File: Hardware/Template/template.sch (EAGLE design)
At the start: 24 parts, among them J1 10144517-042802LF, J2 10144518-041802LF, J3 10144517-042802LF, J4 10144518-041802LF, J6 2X5_0.05_SWD, U6 NCV8170AXV330T2G, U7 ATA6561-GAQW-N

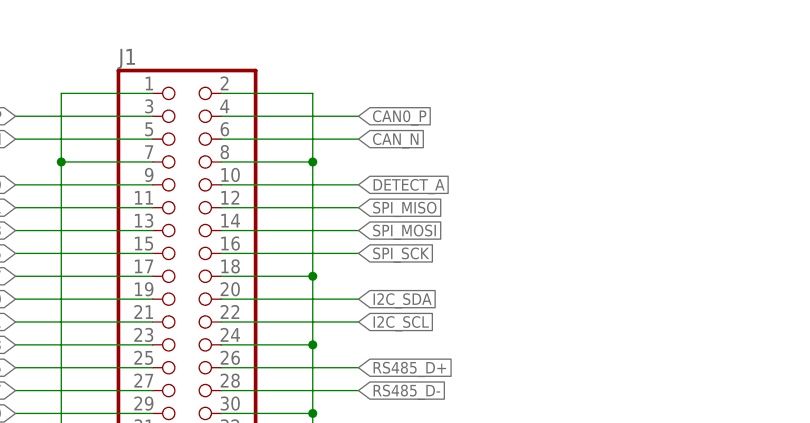
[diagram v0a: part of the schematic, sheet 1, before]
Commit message: fixed power rail naming in template and added inventor drawing
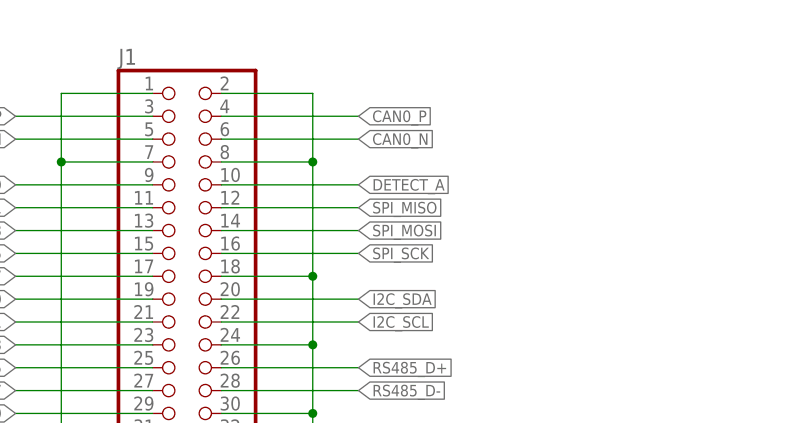
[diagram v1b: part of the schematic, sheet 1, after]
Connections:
- new net +12V: J3.17, J3.19, J3.21, J3.23, J3.25, J3.27, J3.29, J4.17, J4.19, J4.21, J4.23, J4.25, J4.27, J4.29
- net +5V: no longer J3.17, J3.19, J3.21, J3.23, J3.25, J3.27, J3.29, J4.17, J4.19, J4.21, J4.23, J4.25, J4.27, J4.29
- net CAN0_N: now also J1.6
- net CAN_N: no longer J1.6
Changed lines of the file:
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@@
 <?xml version="1.0" encoding="utf-8"?>
 <!DOCTYPE eagle SYSTEM "eagle.dtd">
-<eagle version="9.5.2">
+<eagle version="9.6.0">
 <drawing>
 <settings>
-<setting alwaysvectorfont="no"/>
+<setting alwaysvectorfont="yes"/>
 <setting verticaltext="up"/>
 </settings>
@@
 <net name="CAN_N" class="0">
 <segment>
-<wire x1="38.1" y1="187.96" x2="53.34" y2="187.96" width="0.1524" layer="91"/>
-<label x="53.34" y="187.96" size="1.27" layer="95" xref="yes"/>
-<pinref part="J1" gate="A" pin="6"/>
-</segment>
-<segment>
 <pinref part="U7" gate="G$1" pin="CANL"/>
 <label x="17.78" y="43.18" size="1.27" layer="95" rot="MR0" xref="yes"/>
@@
 <pinref part="J2" gate="A" pin="6"/>
 </segment>
+<segment>
+<wire x1="38.1" y1="187.96" x2="53.34" y2="187.96" width="0.1524" layer="91"/>
+<label x="53.34" y="187.96" size="1.27" layer="95" xref="yes"/>
+<pinref part="J1" gate="A" pin="6"/>
+</segment>
 </net>
 <net name="+5V" class="0">
@@
 <pinref part="P+3" gate="1" pin="+5V"/>
 </segment>
+<segment>
+<wire x1="228.6" y1="149.86" x2="228.6" y2="152.4" width="0.1524" layer="91"/>
+<wire x1="228.6" y1="152.4" x2="228.6" y2="154.94" width="0.1524" layer="91"/>
+<wire x1="228.6" y1="154.94" x2="228.6" y2="157.48" width="0.1524" layer="91"/>
+<wire x1="228.6" y1="157.48" x2="223.52" y2="157.48" width="0.1524" layer="91"/>
+<pinref part="J3" gate="A" pin="31"/>
+<wire x1="228.6" y1="157.48" x2="238.76" y2="157.48" width="0.1524" layer="91"/>
+<junction x="228.6" y="157.48"/>
+<pinref part="J3" gate="A" pin="33"/>
+<wire x1="238.76" y1="154.94" x2="228.6" y2="154.94" width="0.1524" layer="91"/>
+<junction x="228.6" y="154.94"/>
+<pinref part="J3" gate="A" pin="35"/>
+<wire x1="238.76" y1="152.4" x2="228.6" y2="152.4" width="0.1524" layer="91"/>
+<junction x="228.6" y="152.4"/>
+<pinref part="J3" gate="A" pin="37"/>
+<wire x1="238.76" y1="149.86" x2="228.6" y2="149.86" width="0.1524" layer="91"/>
+<pinref part="P+6" gate="1" pin="+5V"/>
+</segment>
+</net>
+<net name="+12V" class="0">
 <segment>
 <wire x1="228.6" y1="175.26" x2="223.52" y2="175.26" width="0.1524" layer="91"/>
@@
 <pinref part="P+2" gate="1" pin="+12V"/>
 </segment>
-<segment>
-<wire x1="228.6" y1="149.86" x2="228.6" y2="152.4" width="0.1524" layer="91"/>
-<wire x1="228.6" y1="152.4" x2="228.6" y2="154.94" width="0.1524" layer="91"/>
-<wire x1="228.6" y1="154.94" x2="228.6" y2="157.48" width="0.1524" layer="91"/>
-<wire x1="228.6" y1="157.48" x2="223.52" y2="157.48" width="0.1524" layer="91"/>
-<pinref part="J3" gate="A" pin="31"/>
-<wire x1="228.6" y1="157.48" x2="238.76" y2="157.48" width="0.1524" layer="91"/>
-<junction x="228.6" y="157.48"/>
-<pinref part="J3" gate="A" pin="33"/>
-<wire x1="238.76" y1="154.94" x2="228.6" y2="154.94" width="0.1524" layer="91"/>
-<junction x="228.6" y="154.94"/>
-<pinref part="J3" gate="A" pin="35"/>
-<wire x1="238.76" y1="152.4" x2="228.6" y2="152.4" width="0.1524" layer="91"/>
-<junction x="228.6" y="152.4"/>
-<pinref part="J3" gate="A" pin="37"/>
-<wire x1="238.76" y1="149.86" x2="228.6" y2="149.86" width="0.1524" layer="91"/>
-<pinref part="P+6" gate="1" pin="+5V"/>
-</segment>
-</net>
+</net>

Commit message: sims and some other stuff...
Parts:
- removed F1: (no value), adafruit:PTCFUSE-1206
- removed U$13, U$9: WIRE-PAD, Wire Pads:WIRE-PAD
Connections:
- removed net +V_BAT_INT: F1.2
- removed net N$16: F1.1, U$13.TP
- net PGND: no longer U$9.TP
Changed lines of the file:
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@@
 <part name="J2" library="BergStak" library_urn="urn:adsk.eagle:library:14049968" deviceset="10144518-04" device="1802LF" package3d_urn="urn:adsk.eagle:package:14050130/2"/>
 <part name="U$12" library="Supply" deviceset="SHIELD" device=""/>
-<part name="U$9" library="Wire Pads" deviceset="WIRE-PAD" device=""/>
-<part name="U$13" library="Wire Pads" deviceset="WIRE-PAD" device=""/>
-<part name="F1" library="adafruit" library_urn="urn:adsk.eagle:library:420" deviceset="PTCFUSE" device="-1206" package3d_urn="urn:adsk.eagle:package:6240569/1"/>
 <part name="R8" library="rcl" library_urn="urn:adsk.eagle:library:334" deviceset="R-US_" device="R0402" package3d_urn="urn:adsk.eagle:package:23547/3"/>
 <part name="U$14" library="Supply" deviceset="SHIELD" device=""/>
@@
 <part name="U$26" library="Supply" deviceset="PGND" device=""/>
 <part name="U$27" library="Supply" deviceset="DGND" device=""/>
-<part name="U$28" library="Supply" deviceset="PGND" device=""/>
 <part name="U$29" library="Supply" deviceset="DGND" device=""/>
 <part name="U$30" library="Supply" deviceset="DGND" device=""/>
@@
 <attribute name="VALUE" x="22.86" y="68.58" size="1.778" layer="96" rot="MR90"/>
 </instance>
-<instance part="U$9" gate="G$1" x="22.86" y="12.7" smashed="yes">
-<attribute name="NAME" x="21.59" y="13.97" size="1.778" layer="95"/>
-</instance>
-<instance part="U$13" gate="G$1" x="22.86" y="22.86" smashed="yes">
-<attribute name="NAME" x="21.59" y="24.13" size="1.778" layer="95"/>
-</instance>
-<instance part="F1" gate="G$1" x="33.02" y="15.24" smashed="yes">
-<attribute name="VALUE" x="29.21" y="13.97" size="1.778" layer="96"/>
-<attribute name="NAME" x="29.21" y="20.32" size="1.778" layer="95"/>
-</instance>
 <instance part="R8" gate="G$1" x="228.6" y="63.5" smashed="yes">
 <attribute name="NAME" x="224.79" y="64.9986" size="1.778" layer="95"/>
@@
 <attribute name="NAME" x="23.9014" y="44.45" size="1.778" layer="95" rot="R90"/>
 <attribute name="VALUE" x="28.702" y="44.45" size="1.778" layer="96" rot="R90"/>
-</instance>
-<instance part="U$28" gate="G$1" x="22.86" y="7.62" smashed="yes">
-<attribute name="VALUE" x="20.32" y="5.08" size="1.778" layer="96"/>
 </instance>
 <instance part="U$29" gate="G$1" x="93.98" y="33.02" smashed="yes">
@@
 </segment>
 </net>
-<net name="+V_BAT_INT" class="0">
-<segment>
-<label x="50.8" y="17.78" size="1.27" layer="95" xref="yes"/>
-<wire x1="38.1" y1="17.78" x2="50.8" y2="17.78" width="0.1524" layer="91"/>
-<pinref part="F1" gate="G$1" pin="2"/>
-</segment>
-</net>
 <net name="P_GOOD" class="0">
 <segment>
@@
 </segment>
 </net>
-<net name="N$16" class="0">
-<segment>
-<pinref part="U$13" gate="G$1" pin="TP"/>
-<wire x1="22.86" y1="20.32" x2="22.86" y2="17.78" width="0.1524" layer="91"/>
-<pinref part="F1" gate="G$1" pin="1"/>
-<wire x1="22.86" y1="17.78" x2="27.94" y2="17.78" width="0.1524" layer="91"/>
-</segment>
-</net>
 <net name="RFU_37" class="0">
 <segment>
@@
 <net name="PGND" class="0">
 <segment>
-<pinref part="U$9" gate="G$1" pin="TP"/>
-<pinref part="U$28" gate="G$1" pin="PGND"/>
-</segment>
-<segment>
 <pinref part="J3" gate="A" pin="2"/>
